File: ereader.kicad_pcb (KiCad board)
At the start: 4 copper layers, 66 x 115 mm, 56 parts, among them J1 USB-C-16P, J2 EPD_FPC_24P, J3 FL_FPC_6P, J4 microSD, J5 Battery_1S, SW1 BTN_A, SW2 BTN_B, SW3 BTN_C, SW4 SLLB510200, U1 ESP32-S3-WROOM-1-N16R8, U2 BQ25628E (PLACEHOLDER-VERIFY), U3 MAX17048 (PLACEHOLDER-VERIFY), U4 LM3630A (PLACEHOLDER-VERIFY), U5 TPS62840 (PLACEHOLDER-VERIFY), U6 USBLC6-2SC6

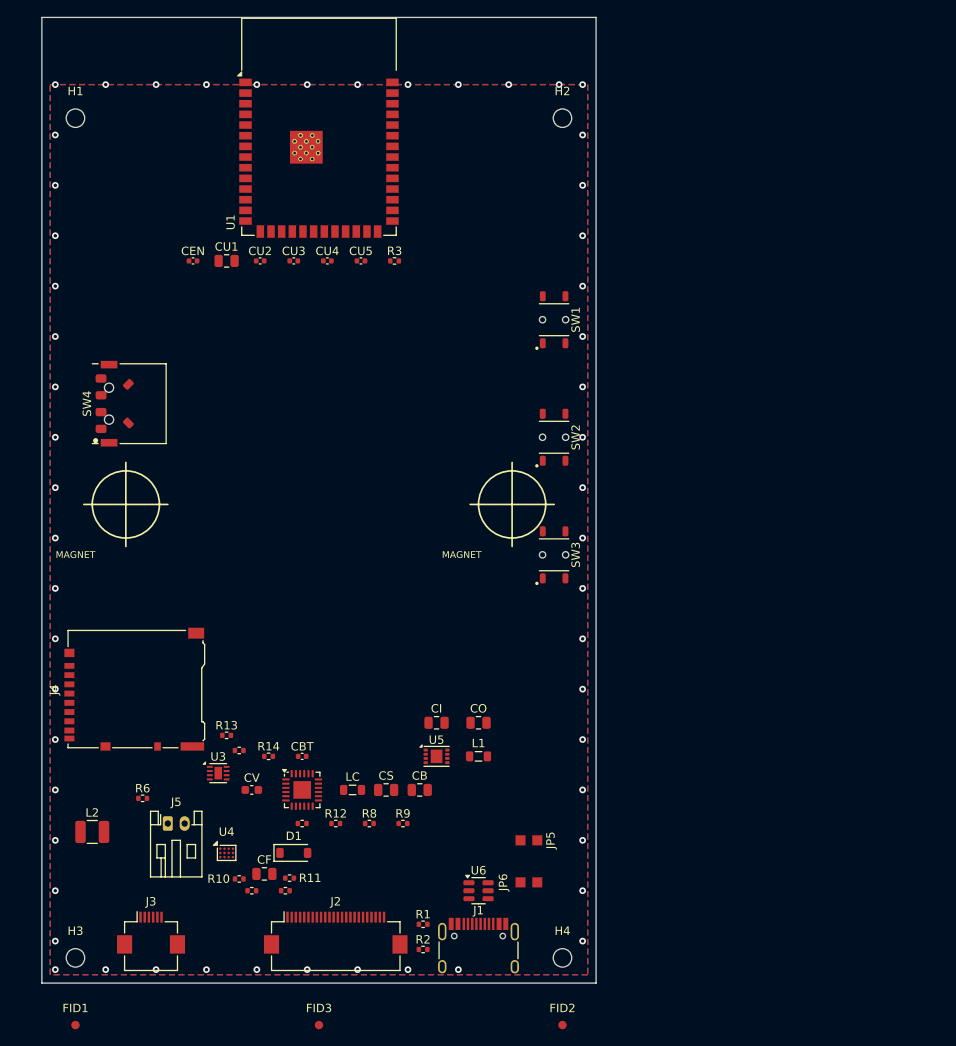
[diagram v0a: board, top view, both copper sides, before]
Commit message: board routed and gerber file generated incl. DRC report
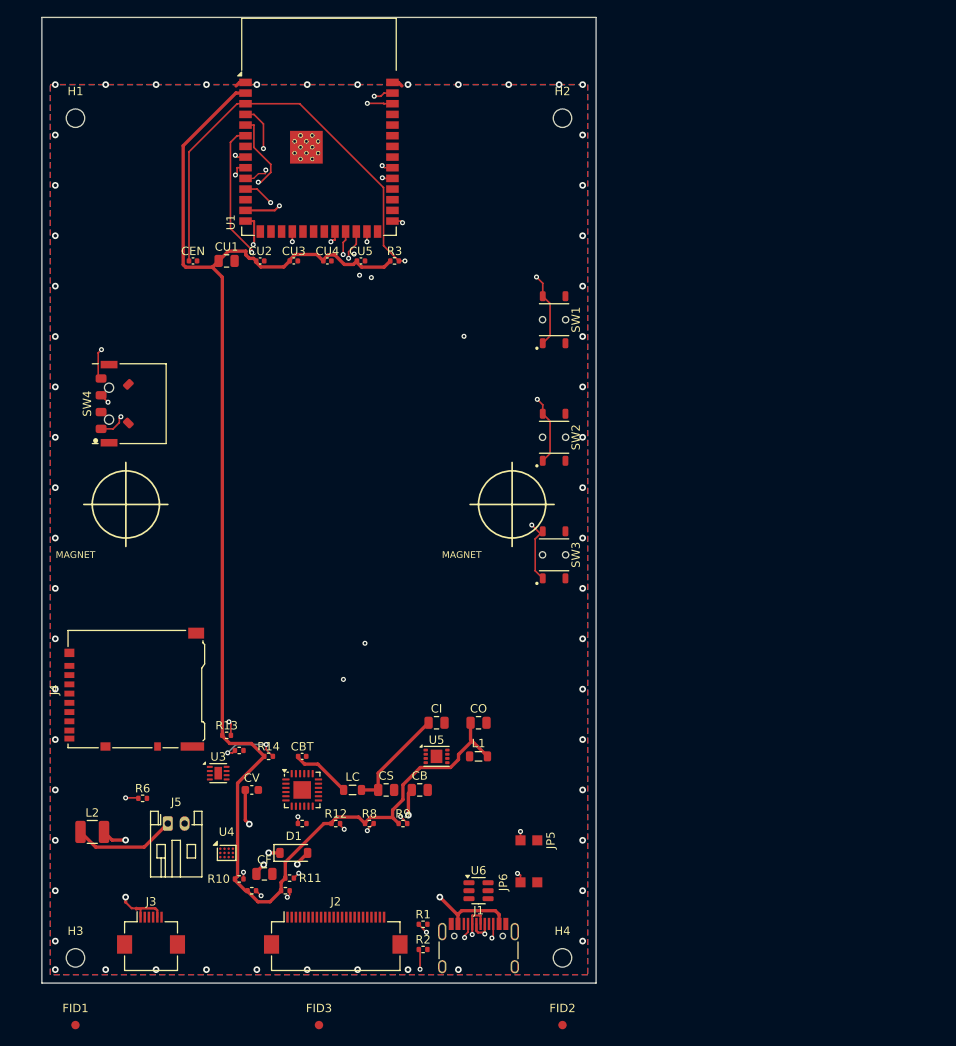
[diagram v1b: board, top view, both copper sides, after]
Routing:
- net +3V3: track 0.00 -> 179.6 mm
- net I2C0_SDA: track 0.00 -> 148.3 mm, vias 0 -> 3
- net EN: track 0.00 -> 132.7 mm, vias 0 -> 2
- net USB_DP: track 0.00 -> 108.8 mm, vias 0 -> 3
- net USB_DM: track 0.00 -> 106.2 mm, vias 0 -> 3
- net SD_CS: track 0.00 -> 96.5 mm, vias 0 -> 2
- net I2C1_SCL: track 0.00 -> 89.0 mm, vias 0 -> 2
- net FL_HWEN: track 0.00 -> 86.8 mm, vias 0 -> 3
- net I2C1_SDA: track 0.00 -> 86.2 mm, vias 0 -> 2
- net I2C0_SCL: track 0.00 -> 85.6 mm, vias 0 -> 3
- net IO0_BOOT: track 0.00 -> 80.7 mm, vias 0 -> 2
- net EPD_CS: track 0.00 -> 80.4 mm, vias 0 -> 2
- net CHG_INT: track 0.00 -> 72.7 mm, vias 0 -> 2
- net CHG_CE: track 0.00 -> 72.5 mm, vias 0 -> 2
- net GAUGE_ALRT: track 0.00 -> 70.9 mm, vias 0 -> 3
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
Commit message: import netlist: add EPD DC-DC + charger support parts
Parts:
- added C4I: 1uF, Capacitor_SMD:C_0402_1005Metric, F.Cu at (101.3, 91.0)
- added CE1: 4.7uF/25V, Capacitor_SMD:C_0805_2012Metric, F.Cu at (94.7, 81.5)
- added CE10: 4.7uF/25V, Capacitor_SMD:C_0805_2012Metric, F.Cu at (94.7, 99.6)
- added CE2: 4.7uF/25V, Capacitor_SMD:C_0805_2012Metric, F.Cu at (94.7, 84.5)
- added CE3: 4.7uF/25V, Capacitor_SMD:C_0805_2012Metric, F.Cu at (94.7, 87.5)
- added CE4: 4.7uF/25V, Capacitor_SMD:C_0805_2012Metric, F.Cu at (94.7, 90.5)
- added CE5: 4.7uF/25V, Capacitor_SMD:C_0805_2012Metric, F.Cu at (94.7, 93.5)
- added CE6: 4.7uF/25V, Capacitor_SMD:C_0805_2012Metric, F.Cu at (94.7, 96.6)
- added CE7: 1uF/25V, Capacitor_SMD:C_0603_1608Metric, F.Cu at (104.7, 81.3)
- added CE8: 1uF/25V, Capacitor_SMD:C_0603_1608Metric, F.Cu at (104.7, 83.8)
- added CE9: 1uF/25V, Capacitor_SMD:C_0603_1608Metric, F.Cu at (104.7, 86.3)
- added CGA: 0.1uF, Capacitor_SMD:C_0402_1005Metric, F.Cu at (101.3, 93.0)
- added CGB: 1uF, Capacitor_SMD:C_0402_1005Metric, F.Cu at (101.3, 95.0)
- added CPM: 10uF, Capacitor_SMD:C_0805_2012Metric, F.Cu at (94.7, 102.6)
- added CPM2: 0.1uF, Capacitor_SMD:C_0402_1005Metric, F.Cu at (101.3, 96.9)
- added CRG: 4.7uF, Capacitor_SMD:C_0603_1608Metric, F.Cu at (104.7, 88.8)
- added DE1: MBR0530, Diode_SMD:D_SOD-123, F.Cu at (99.9, 81.7)
- added DE2: MBR0530, Diode_SMD:D_SOD-123, F.Cu at (99.9, 85.0)
- added DE3: MBR0530, Diode_SMD:D_SOD-123, F.Cu at (99.9, 88.4)
- added LE: 47uH, Inductor_SMD:L_1210_3225Metric, F.Cu at (102.7, 100.0)
- added QE: Si1308EDL, Package_TO_SOT_SMD:SOT-23, F.Cu at (105.2, 92.3)
- added R16: 267k, Resistor_SMD:R_0402_1005Metric, F.Cu at (98.4, 91.0)
- added R17: 1.65k, Resistor_SMD:R_0402_1005Metric, F.Cu at (98.4, 93.0)
- added RE1: 2.2R, Resistor_SMD:R_0402_1005Metric, F.Cu at (98.4, 95.0)
- added RE2: 1M, Resistor_SMD:R_0402_1005Metric, F.Cu at (98.4, 97.0)
- CB, CF, CI, CO, CS, CU1: footprint C_0805_2012Metric -> Capacitor_SMD:C_0805_2012Metric
- CBT, CEN, CU2, CU3, CU4, CU5: footprint C_0402_1005Metric -> Capacitor_SMD:C_0402_1005Metric
- CV: footprint C_0603_1608Metric -> Capacitor_SMD:C_0603_1608Metric
- D1: footprint D_SOD-123 -> Diode_SMD:D_SOD-123
- J1: footprint USB_C_Receptacle_HRO_TYPE-C-31-M-12 -> Connector_USB:USB_C_Receptacle_HRO_TYPE-C-31-M-12
- J2: footprint Hirose_FH12-24S-0.5SH_1x24-1MP_P0.50mm_Horizontal -> Connector_FFC-FPC:Hirose_FH12-24S-0.5SH_1x24-1MP_P0.50mm_Horizontal
- J3: footprint Hirose_FH12-6S-0.5SH_1x06-1MP_P0.50mm_Horizontal -> Connector_FFC-FPC:Hirose_FH12-6S-0.5SH_1x06-1MP_P0.50mm_Horizontal
- J4: footprint microSD_HC_Hirose_DM3AT-SF-PEJM5 -> ereader:HRS_DM3AT-SF-PEJM5
- J5: footprint JST_PH_S2B-PH-K_1x02_P2.00mm_Horizontal -> Connector_JST:JST_PH_S2B-PH-K_1x02_P2.00mm_Horizontal
- L1, LC: footprint L_0805_2012Metric -> Inductor_SMD:L_0805_2012Metric
- L2: footprint L_1210_3225Metric -> Inductor_SMD:L_1210_3225Metric
- R1, R10, R11, R12, R13, R14, R15, R2, R3, R4, R5, R6, R7, R8, R9: footprint R_0402_1005Metric -> Resistor_SMD:R_0402_1005Metric
- U1: footprint ESP32-S3-WROOM-1 -> RF_Module:ESP32-S3-WROOM-1
- U2: value BQ25628E (PLACEHOLDER-VERIFY) -> BQ25628E; footprint HVQFN-24-1EP_4x4mm_P0.5mm_EP2.1x2.1mm -> ereader:WQFN-HR18__RYK_TEX
- U3: value MAX17048 (PLACEHOLDER-VERIFY) -> MAX17048; footprint DFN-8-1EP_2x2mm_P0.5mm_EP0.9x1.5mm -> ereader:SON50P200X200X80-9N
- U4: value LM3630A (PLACEHOLDER-VERIFY) -> LM3630A; footprint Maxim_WLP-12 -> ereader:BGA12N50P4X3_196X146X62
- U5: value TPS62840 (PLACEHOLDER-VERIFY) -> TPS62840; footprint SON-8-1EP_3x2mm_P0.5mm_EP1.4x1.6mm -> ereader:SON50P200X200X80-9N
- U6: footprint SOT-23-6 -> Package_TO_SOT_SMD:SOT-23-6
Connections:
- D1 pad 1: FL_SW -> FL_OUT
- D1 pad 2: FL_OUT -> FL_SW
- J2 pad 10: (no net) -> EPD_RST
- J2 pad 11: (no net) -> EPD_DC
- J2 pad 12: (no net) -> EPD_CS
- J2 pad 13: (no net) -> EPD_SCLK
- J2 pad 14: (no net) -> EPD_MOSI
- J2 pad 15: (no net) -> +3V3
- J2 pad 16: (no net) -> +3V3
- J2 pad 17: (no net) -> GND
- J2 pad 18: (no net) -> EPD_VDD
- J2 pad 2: (no net) -> EPD_GDR
- J2 pad 20: (no net) -> EPD_VSH1
- J2 pad 21: (no net) -> EPD_VGH
- J2 pad 22: (no net) -> EPD_VSL
- J2 pad 23: (no net) -> EPD_VGL
- J2 pad 24: (no net) -> EPD_VCOM
- J2 pad 3: (no net) -> EPD_RESE
- J2 pad 5: (no net) -> EPD_VSH2
- J2 pad 8: (no net) -> GND
- J2 pad 9: (no net) -> EPD_BUSY
- J4 pad 2: (no net) -> SD_CS
- J4 pad 3: (no net) -> SD_MOSI
- J4 pad 4: (no net) -> +3V3
- J4 pad 5: (no net) -> SD_SCK
- J4 pad 6: (no net) -> GND
- J4 pad 7: (no net) -> SD_MISO
- R14 pad 1: +3V3 -> TS_BIAS
- U2 pad 1: (no net) -> CHG_BTST
- U2 pad 11: (no net) -> CHG_INT
- U2 pad 12: (no net) -> I2C0_SDA
- U2 pad 13: (no net) -> I2C0_SCL
- U2 pad 14: (no net) -> CHG_CE
- U2 pad 15: (no net) -> GND
- U2 pad 16: (no net) -> CHG_SW
- U2 pad 17: (no net) -> PMID
- U2 pad 18: (no net) -> +VBUS
- U2 pad 2: (no net) -> REGN
- U2 pad 4: (no net) -> ILIM
- U2 pad 5: (no net) -> TS_BIAS
- U2 pad 6: (no net) -> TS
- U2 pad 8: (no net) -> +VBAT
- U2 pad 9: (no net) -> +SYS
- U3 pad 1: (no net) -> GND
- U3 pad 2: (no net) -> +VBAT
- U3 pad 3: (no net) -> +VBAT
- U3 pad 4: (no net) -> GND
- U3 pad 5: (no net) -> GAUGE_ALRT
- U3 pad 6: (no net) -> GND
- U3 pad 7: (no net) -> I2C0_SCL
- U3 pad 8: (no net) -> I2C0_SDA
- U3 pad 9: (no net) -> GND
- U4 pad A1: (no net) -> I2C1_SDA
- U4 pad A2: (no net) -> I2C1_SCL
- U4 pad A3: (no net) -> FL_SW
- U4 pad B1: (no net) -> FL_HWEN
- U4 pad B3: (no net) -> GND
- U4 pad C1: (no net) -> GND
- U4 pad C2: (no net) -> GND
- U4 pad C3: (no net) -> +VBAT
- U5 pad 1: (no net) -> GND
- U5 pad 2: (no net) -> +SYS
- U5 pad 3: (no net) -> GND
- U5 pad 4: (no net) -> +SYS
- U5 pad 5: (no net) -> VSET
- U5 pad 6: (no net) -> GND
- U5 pad 7: (no net) -> BUCK_SW
- U5 pad 8: (no net) -> +3V3
- U5 pad 9: (no net) -> GND
- U6 pad 1: (no net) -> USB_DP
- U6 pad 2: (no net) -> GND
- U6 pad 3: (no net) -> USB_DM
- U6 pad 4: (no net) -> USB_DM
- U6 pad 5: (no net) -> +VBUS
- U6 pad 6: (no net) -> USB_DP
